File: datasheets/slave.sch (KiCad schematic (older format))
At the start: 22 parts, among them J1 Screw_Terminal_1x02, J2 Screw_Terminal_1x03, Q1 IRFU9024N, Q2 IRFU9024N, Q3 IRFU9024N, U1 PC817, U2 PC817, U3 PC817, U4 nRF24L01, U5 Arduino_Nano

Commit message: Исправление ошибок в схемах
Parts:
- added C1: C, Capacitors_THT:C_Disc_D6.0mm_W2.5mm_P5.00mm, symbol C
- added C2: CP, w_capacitors:CP_5x11mm, symbol CP
- added J3: Screw_Terminal_1x02, w_conn_screw:mors_2p, symbol Screw_Terminal_1x02
- added U6: KA378R33, TO_SOT_Packages_THT:TO-220-4_Vertical, symbol KA378R33
- J1: footprint Connectors_Terminal_Blocks:TerminalBlock_Pheonix_MKDS1.5-2pol -> w_conn_screw:mors_2p
- J2: footprint Connectors_Terminal_Blocks:TerminalBlock_Pheonix_MKDS1.5-3pol -> w_conn_screw:mors_3p
- R1: value R -> 470; footprint Resistors_THT:R_Axial_DIN0207_L6.3mm_D2.5mm_P2.54mm_Vertical -> Resistors_THT:R_Axial_DIN0207_L6.3mm_D2.5mm_P10.16mm_Horizontal
- R2: value R -> 10k
- R3: value R -> 100
- R4, R5: footprint Resistors_THT:R_Axial_DIN0207_L6.3mm_D2.5mm_P2.54mm_Vertical -> Resistors_THT:R_Axial_DIN0207_L6.3mm_D2.5mm_P10.16mm_Horizontal
- U4: footprint (none) -> nRF24x:nRF24L01-NA
- U5: footprint (none) -> arduino:ArduinoNano
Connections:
- net labels added: 3V3, D_VCC
- wire segments 64 -> 77
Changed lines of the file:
@@
 EESchema Schematic File Version 2
+LIBS:slave-rescue
 LIBS:power
 LIBS:device
@@
 Wire Wire Line
 	9400 2850 9500 2850
-NoConn ~ 10250 2450
+NoConn ~ 10250 2850
 Wire Wire Line
 	10150 2250 10150 2450
@@
 F 3 "" H 10050 2650 50  0000 C CNN
 	1    10050 2650
-	1    0    0    -1
+	1    0    0    1
 $EndComp
 Wire Wire Line
@@
 P 8600 2650
 F 0 "R1" V 8680 2650 50  0000 C CNN
-F 1 "R" V 8600 2650 50  0000 C CNN
-F 2 "Resistors_THT:R_Axial_DIN0207_L6.3mm_D2.5mm_P2.54mm_Vertical" V 8530 2650 50  0001 C CNN
+F 1 "470" V 8600 2650 50  0000 C CNN
+F 2 "Resistors_THT:R_Axial_DIN0207_L6.3mm_D2.5mm_P10.16mm_Horizontal" V 8530 2650 50  0001 C CNN
 F 3 "" H 8600 2650 50  0000 C CNN
 	1    8600 2650
@@
 P 9450 2450
 F 0 "R2" V 9530 2450 50  0000 C CNN
-F 1 "R" V 9450 2450 50  0000 C CNN
+F 1 "10k" V 9450 2450 50  0000 C CNN
 F 2 "Resistors_THT:R_Axial_DIN0207_L6.3mm_D2.5mm_P2.54mm_Vertical" V 9380 2450 50  0001 C CNN
 F 3 "" H 9450 2450 50  0000 C CNN
@@
 P 9650 2650
 F 0 "R3" V 9730 2650 50  0000 C CNN
-F 1 "R" V 9650 2650 50  0000 C CNN
+F 1 "100" V 9650 2650 50  0000 C CNN
 F 2 "Resistors_THT:R_Axial_DIN0207_L6.3mm_D2.5mm_P2.54mm_Vertical" V 9580 2650 50  0001 C CNN
 F 3 "" H 9650 2650 50  0000 C CNN
@@
 Wire Wire Line
 	9400 3950 9500 3950
-NoConn ~ 10250 3550
+NoConn ~ 10250 3950
 Wire Wire Line
 	10150 3350 10150 3550
@@
 F 3 "" H 10050 3750 50  0000 C CNN
 	1    10050 3750
-	1    0    0    -1
+	1    0    0    1
 $EndComp
 Wire Wire Line
@@
 F 0 "R4" V 8680 3750 50  0000 C CNN
 F 1 "R" V 8600 3750 50  0000 C CNN
-F 2 "Resistors_THT:R_Axial_DIN0207_L6.3mm_D2.5mm_P2.54mm_Vertical" V 8530 3750 50  0001 C CNN
+F 2 "Resistors_THT:R_Axial_DIN0207_L6.3mm_D2.5mm_P10.16mm_Horizontal" V 8530 3750 50  0001 C CNN
 F 3 "" H 8600 3750 50  0000 C CNN
 	1    8600 3750
@@
 Wire Wire Line
 	9400 5100 9500 5100
-NoConn ~ 10250 4700
+NoConn ~ 10250 5100
 Wire Wire Line
 	10150 4500 10150 4700
@@
 F 3 "" H 10050 4900 50  0000 C CNN
 	1    10050 4900
-	1    0    0    -1
+	1    0    0    1
 $EndComp
 Wire Wire Line
@@
 F 0 "R5" V 8680 4900 50  0000 C CNN
 F 1 "R" V 8600 4900 50  0000 C CNN
-F 2 "Resistors_THT:R_Axial_DIN0207_L6.3mm_D2.5mm_P2.54mm_Vertical" V 8530 4900 50  0001 C CNN
+F 2 "Resistors_THT:R_Axial_DIN0207_L6.3mm_D2.5mm_P10.16mm_Horizontal" V 8530 4900 50  0001 C CNN
 F 3 "" H 8600 4900 50  0000 C CNN
 	1    8600 4900
@@
 P 9200 1300
 F 0 "J1" H 9200 1550 50  0000 C TNN
-F 1 "Screw_Terminal_1x02" V 9050 1300 50  0000 C TNN
-F 2 "Connectors_Terminal_Blocks:TerminalBlock_Pheonix_MKDS1.5-2pol" H 9200 1075 50  0001 C CNN
+F 1 "Screw_Terminal_1x02" V 9050 1300 50  0001 C TNN
+F 2 "w_conn_screw:mors_2p" H 9200 1075 50  0001 C CNN
 F 3 "" H 9175 1300 50  0001 C CNN
 	1    9200 1300
-	-1   0    0    -1
+	-1   0    0    1
 $EndComp
 Wire Wire Line
@@
 P 10300 1400
 F 0 "J2" H 10300 1750 50  0000 C TNN
-F 1 "Screw_Terminal_1x03" V 10150 1400 50  0000 C TNN
-F 2 "Connectors_Terminal_Blocks:TerminalBlock_Pheonix_MKDS1.5-3pol" H 10300 1075 50  0001 C CNN
+F 1 "Screw_Terminal_1x03" V 10150 1400 50  0001 C TNN
+F 2 "w_conn_screw:mors_3p" H 10300 1075 50  0001 C CNN
 F 3 "" H 10275 1500 50  0001 C CNN
 	1    10300 1400
@@
 OUT_1
 Text Label 9800 1200 0    60   ~ 0
-OUT_1
+OUT_3
 Text Label 9800 1400 0    60   ~ 0
 OUT_2
 Text Label 9800 1600 0    60   ~ 0
-OUT_3
+OUT_1
 $Comp
 L Arduino_Nano U5
@@
 F 0 "U5" H 6700 5200 60  0000 C CNN
 F 1 "Arduino_Nano" H 6700 5300 60  0000 C CNN
-F 2 "" H 6700 5200 60  0001 C CNN
+F 2 "arduino:ArduinoNano" H 6700 5200 60  0001 C CNN
 F 3 "" H 6700 5200 60  0001 C CNN
 	1    6700 4400
@@
 	8450 2650 8200 2650
 Text Label 5700 4300 0    60   ~ 0
-IN_1
+IN_3
 Text Label 5700 4400 0    60   ~ 0
 IN_2
 Text Label 5700 4500 0    60   ~ 0
-IN_3
+IN_1
 Text Label 8200 2650 0    60   ~ 0
 IN_1
@@
 Text Label 8200 4900 0    60   ~ 0
 IN_3
-$Comp
-L nRF24L01 U4
-U 1 1 59AE991B
-P 6500 3100
-F 0 "U4" H 6500 3300 60  0000 C CNN
-F 1 "nRF24L01" H 6500 3400 60  0000 C CNN
-F 2 "" H 6500 4050 60  0001 C CNN
-F 3 "" H 6500 4050 60  0001 C CNN
-	1    6500 3100
-	1    0    0    -1
-$EndComp
 Wire Wire Line
 	6000 5100 5700 5100
@@
 NoConn ~ 7400 4000
 NoConn ~ 7400 3900
+$Comp
+L nRF24L01 U4
+U 1 1 59AE849D
+P 6500 3100
+F 0 "U4" H 6500 3450 60  0000 C CNN
+F 1 "nRF24L01" H 6500 3350 60  0000 C CNN
+F 2 "nRF24x:nRF24L01-NA" H 6400 3900 60  0001 C CNN
+F 3 "" H 6400 3900 60  0001 C CNN
+	1    6500 3100
+	1    0    0    -1
+$EndComp
+$Comp
+L Screw_Terminal_1x02 J3
+U 1 1 59AE90CE
+P 8100 1300
+F 0 "J3" H 8100 1550 50  0000 C TNN
+F 1 "Screw_Terminal_1x02" V 7950 1300 50  0001 C TNN
+F 2 "w_conn_screw:mors_2p" H 8100 1075 50  0001 C CNN
+F 3 "" H 8075 1300 50  0001 C CNN
+	1    8100 1300
+	-1   0    0    1
+$EndComp
+Wire Wire Line
+	6000 4000 5700 4000
+Text Label 5700 4000 0    60   ~ 0
+D_GND
+Wire Wire Line
+	7900 1200 7600 1200
+Wire Wire Line
+	7900 1400 7600 1400
+Text Label 7600 1200 0    60   ~ 0
+D_VCC
+Text Label 7600 1400 0    60   ~ 0
+D_GND
+Wire Wire Line
+	7400 3700 7700 3700
+Text Label 7700 3700 2    60   ~ 0
+D_VCC
+Wire Wire Line
+	7000 3000 7300 3000
+Text Label 7300 3000 2    60   ~ 0
+3V3
+$Comp
+L KA378R33 U6
+U 1 1 59AEA7DB
+P 6400 1250
+F 0 "U6" H 6200 1450 50  0000 C CNN
+F 1 "KA378R33" H 6350 1450 50  0000 L CNN
+F 2 "TO_SOT_Packages_THT:TO-220-4_Vertical" H 6400 1350 50  0001 C CIN
+F 3 "" H 6400 1250 50  0001 C CNN
+	1    6400 1250
+	1    0    0    -1
+$EndComp
+Wire Wire Line
+	6000 1200 5700 1200
+Wire Wire Line
+	6800 1200 7100 1200
+Wire Wire Line
+	5700 1350 6000 1350
+Wire Wire Line
+	6400 1550 6400 1850
+Text Label 5700 1200 0    60   ~ 0
+D_VCC
+Text Label 5700 1350 0    60   ~ 0
+D_VCC
+Text Label 7100 1200 2    60   ~ 0
+3V3
+Text Label 6400 1850 1    60   ~ 0
+D_GND
+$Comp
+L CP C2
+U 1 1 59AEA26C
+P 6900 1400
+F 0 "C2" H 6925 1500 50  0000 L CNN
+F 1 "CP" H 6925 1300 50  0000 L CNN
+F 2 "w_capacitors:CP_5x11mm" H 6938 1250 50  0001 C CNN
+F 3 "" H 6900 1400 50  0001 C CNN
+	1    6900 1400
+	1    0    0    -1
+$EndComp
+$Comp
+L C C1
+U 1 1 59AEA4A0
+P 5900 1600
+F 0 "C1" H 5925 1700 50  0000 L CNN
+F 1 "C" H 5925 1500 50  0000 L CNN
+F 2 "Capacitors_THT:C_Disc_D6.0mm_W2.5mm_P5.00mm" H 5938 1450 50  0001 C CNN
+F 3 "" H 5900 1600 50  0001 C CNN
+	1    5900 1600
+	1    0    0    -1
+$EndComp
+Wire Wire Line
+	5900 1450 5900 1350
+Connection ~ 5900 1350
+Wire Wire Line
+	5900 1750 6900 1750
+Connection ~ 6400 1750
+Wire Wire Line
+	6900 1750 6900 1550
+Wire Wire Line
+	6900 1250 6900 1200
+Connection ~ 6900 1200
 $EndSCHEMATC

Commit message: Правка схем
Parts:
- removed U5: Arduino_Nano, arduino:ArduinoNano, symbol Arduino_Nano
- added U5: ArduinoNano, Modules:Arduino_Nano, symbol ArduinoNano
- D1, D2, D3: footprint user_diodes:D_DO-41_SOD81_P12.70mm_Horizontal -> Diodes_THT:D_DO-41_SOD81_P12.70mm_Horizontal
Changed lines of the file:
@@
 EESchema Schematic File Version 2
-LIBS:slave-rescue
 LIBS:power
 LIBS:device
@@
 LIBS:contrib
 LIBS:valves
+LIBS:arduino
+LIBS:nrf
 LIBS:user_transistors
 LIBS:user_diodes
-LIBS:arduino
-LIBS:nrf
 LIBS:slave-cache
-EELAYER 25 0
+EELAYER 26 0
 EELAYER END
 $Descr A4 11693 8268
@@
 Wire Wire Line
 	10150 3250 10150 3300
-Wire Wire Line
-	10150 2850 10150 2950
 $Comp
 L 1N4007 D1
@@
 F 0 "D1" H 10150 3200 50  0000 C CNN
 F 1 "1N4007" H 10150 3000 50  0000 C CNN
-F 2 "user_diodes:D_DO-41_SOD81_P12.70mm_Horizontal" H 10150 3100 50  0001 C CNN
+F 2 "Diodes_THT:D_DO-41_SOD81_P12.70mm_Horizontal" H 10150 3100 50  0001 C CNN
 F 3 "" H 10150 3100 50  0000 C CNN
 	1    10150 3100
@@
 Wire Wire Line
 	10150 4350 10150 4400
-Wire Wire Line
-	10150 3950 10150 4050
 $Comp
 L 1N4007 D2
@@
 F 0 "D2" H 10150 4300 50  0000 C CNN
 F 1 "1N4007" H 10150 4100 50  0000 C CNN
-F 2 "user_diodes:D_DO-41_SOD81_P12.70mm_Horizontal" H 10150 4200 50  0001 C CNN
+F 2 "Diodes_THT:D_DO-41_SOD81_P12.70mm_Horizontal" H 10150 4200 50  0001 C CNN
 F 3 "" H 10150 4200 50  0000 C CNN
 	1    10150 4200
@@
 Wire Wire Line
 	10150 5500 10150 5550
-Wire Wire Line
-	10150 5100 10150 5200
 $Comp
 L 1N4007 D3
@@
 F 0 "D3" H 10150 5450 50  0000 C CNN
 F 1 "1N4007" H 10150 5250 50  0000 C CNN
-F 2 "user_diodes:D_DO-41_SOD81_P12.70mm_Horizontal" H 10150 5350 50  0001 C CNN
+F 2 "Diodes_THT:D_DO-41_SOD81_P12.70mm_Horizontal" H 10150 5350 50  0001 C CNN
 F 3 "" H 10150 5350 50  0000 C CNN
 	1    10150 5350
@@
 Text Label 9800 1600 0    60   ~ 0
 OUT_1
-$Comp
-L Arduino_Nano U5
-U 1 1 59AE7866
-P 6700 4400
-F 0 "U5" H 6700 5200 60  0000 C CNN
-F 1 "Arduino_Nano" H 6700 5300 60  0000 C CNN
-F 2 "arduino:ArduinoNano" H 6700 5200 60  0001 C CNN
-F 3 "" H 6700 5200 60  0001 C CNN
-	1    6700 4400
-	1    0    0    -1
-$EndComp
-Wire Wire Line
-	6000 4300 5700 4300
-Wire Wire Line
-	6000 4400 5700 4400
-Wire Wire Line
-	6000 4500 5700 4500
+Wire Wire Line
+	5700 4300 6200 4300
+Wire Wire Line
+	5700 4400 6200 4400
+Wire Wire Line
+	5700 4500 6200 4500
 Wire Wire Line
 	8450 4900 8200 4900
@@
 IN_3
 Wire Wire Line
-	6000 5100 5700 5100
-Wire Wire Line
-	6000 5000 5700 5000
-Wire Wire Line
-	6000 4900 5700 4900
-Wire Wire Line
-	6000 4800 5700 4800
-Wire Wire Line
-	6000 4100 5700 4100
-Wire Wire Line
-	7400 5100 7700 5100
+	5700 5100 6200 5100
+Wire Wire Line
+	5700 5000 6200 5000
+Wire Wire Line
+	5700 4900 6200 4900
+Wire Wire Line
+	5700 4800 6200 4800
+Wire Wire Line
+	5700 4100 6200 4100
+Wire Wire Line
+	7200 5100 7700 5100
 Wire Wire Line
 	6000 3300 5700 3300
@@
 SCN/D9
 Wire Wire Line
-	7400 3800 7700 3800
+	7200 3800 7700 3800
 Text Label 7700 3800 2    60   ~ 0
 D_GND
@@
 Text Label 5700 3000 0    60   ~ 0
 D_GND
-NoConn ~ 6000 3700
-NoConn ~ 6000 3800
-NoConn ~ 6000 3900
-NoConn ~ 6000 4200
-NoConn ~ 6000 4600
-NoConn ~ 6000 4700
-NoConn ~ 7400 5000
-NoConn ~ 7400 4900
-NoConn ~ 7400 4800
-NoConn ~ 7400 4700
-NoConn ~ 7400 4600
-NoConn ~ 7400 4500
-NoConn ~ 7400 4400
-NoConn ~ 7400 4300
-NoConn ~ 7400 4200
-NoConn ~ 7400 4100
-NoConn ~ 7400 4000
-NoConn ~ 7400 3900
+NoConn ~ 6200 4200
+NoConn ~ 6200 4600
+NoConn ~ 6200 4700
 $Comp
 L nRF24L01 U4
@@
 $EndComp
 Wire Wire Line
-	6000 4000 5700 4000
+	5700 4000 6200 4000
 Text Label 5700 4000 0    60   ~ 0
 D_GND
@@
 D_GND
 Wire Wire Line
-	7400 3700 7700 3700
+	7200 3700 7700 3700
 Text Label 7700 3700 2    60   ~ 0
 D_VCC
@@
 	6900 1250 6900 1200
 Connection ~ 6900 1200
+$Comp
+L ArduinoNano U5
+U 1 1 59BC9DC0
+P 6700 4000
+F 0 "U5" H 6700 4547 60  0000 C CNN
+F 1 "ArduinoNano" H 6700 4441 60  0000 C CNN
+F 2 "Modules:Arduino_Nano" H 6650 4550 60  0001 C CNN
+F 3 "" H 6650 4550 60  0001 C CNN
+	1    6700 4000
+	1    0    0    -1
+$EndComp
+NoConn ~ 6200 3700
+NoConn ~ 6200 3800
+NoConn ~ 6200 3900
+NoConn ~ 7200 5000
+NoConn ~ 7200 4900
+NoConn ~ 7200 4800
+NoConn ~ 7200 4700
+NoConn ~ 7200 4600
+NoConn ~ 7200 4500
+NoConn ~ 7200 4400
+NoConn ~ 7200 4300
+NoConn ~ 7200 4200
+NoConn ~ 7200 4100
+NoConn ~ 7200 4000
+NoConn ~ 7200 3900
+Wire Wire Line
+	10150 5100 10150 5200
+Wire Wire Line
+	10150 3950 10150 4050
+Wire Wire Line
+	10150 2850 10150 2950
 $EndSCHEMATC

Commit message: Добавление библиотек компонентов для KiCad.
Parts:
- J1, J3: symbol Screw_Terminal_1x02 -> Screw_Terminal_01x02
- J2: symbol Screw_Terminal_1x03 -> Screw_Terminal_01x03
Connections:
- wire segments 77 -> 78
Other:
- moved on the sheet: C2
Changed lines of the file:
@@
 LIBS:arduino
 LIBS:nrf
+LIBS:user_diodes
 LIBS:user_transistors
-LIBS:user_diodes
 LIBS:slave-cache
-EELAYER 26 0
+EELAYER 25 0
 EELAYER END
 $Descr A4 11693 8268
@@
 P_VCC
 $Comp
-L Screw_Terminal_1x02 J1
+L Screw_Terminal_01x02 J1
 U 1 1 59ADE9CB
 P 9200 1300
@@
 F 3 "" H 9175 1300 50  0001 C CNN
 	1    9200 1300
-	-1   0    0    1
+	1    0    0    1
 $EndComp
 Wire Wire Line
 	9000 1200 8700 1200
 Wire Wire Line
-	9000 1400 8700 1400
+	9000 1300 8700 1300
 Text Label 8700 1200 0    60   ~ 0
 P_VCC
-Text Label 8700 1400 0    60   ~ 0
-P_GND
-$Comp
-L Screw_Terminal_1x03 J2
-U 1 1 59AE55A4
-P 10300 1400
-F 0 "J2" H 10300 1750 50  0000 C TNN
-F 1 "Screw_Terminal_1x03" V 10150 1400 50  0001 C TNN
-F 2 "w_conn_screw:mors_3p" H 10300 1075 50  0001 C CNN
-F 3 "" H 10275 1500 50  0001 C CNN
-	1    10300 1400
-	-1   0    0    1
-$EndComp
-Wire Wire Line
-	10100 1200 9700 1200
-Wire Wire Line
-	10100 1400 9700 1400
-Wire Wire Line
-	10100 1600 9700 1600
+Text Label 8700 1300 0    60   ~ 0
+P_GND
+Wire Wire Line
+	10050 1200 9650 1200
+Wire Wire Line
+	10050 1300 9650 1300
+Wire Wire Line
+	10050 1400 9650 1400
 Wire Wire Line
 	10150 2900 10550 2900
@@
 Text Label 10250 2900 0    60   ~ 0
 OUT_1
-Text Label 9800 1200 0    60   ~ 0
+Text Label 9750 1200 0    60   ~ 0
 OUT_3
-Text Label 9800 1400 0    60   ~ 0
+Text Label 9750 1300 0    60   ~ 0
 OUT_2
-Text Label 9800 1600 0    60   ~ 0
+Text Label 9750 1400 0    60   ~ 0
 OUT_1
 Wire Wire Line
@@
 $EndComp
 $Comp
-L Screw_Terminal_1x02 J3
+L Screw_Terminal_01x02 J3
 U 1 1 59AE90CE
 P 8100 1300
@@
 F 3 "" H 8075 1300 50  0001 C CNN
 	1    8100 1300
-	-1   0    0    1
+	1    0    0    1
 $EndComp
 Wire Wire Line
@@
 	7900 1200 7600 1200
 Wire Wire Line
-	7900 1400 7600 1400
+	7900 1300 7600 1300
 Text Label 7600 1200 0    60   ~ 0
 D_VCC
-Text Label 7600 1400 0    60   ~ 0
+Text Label 7600 1300 0    60   ~ 0
 D_GND
 Wire Wire Line
@@
 $EndComp
 Wire Wire Line
-	6000 1200 5700 1200
-Wire Wire Line
-	6800 1200 7100 1200
-Wire Wire Line
-	5700 1350 6000 1350
+	5700 1150 6100 1150
+Wire Wire Line
+	6700 1150 7100 1150
+Wire Wire Line
+	5700 1300 6100 1300
 Wire Wire Line
 	6400 1550 6400 1850
-Text Label 5700 1200 0    60   ~ 0
+Text Label 5700 1150 0    60   ~ 0
 D_VCC
-Text Label 5700 1350 0    60   ~ 0
+Text Label 5700 1300 0    60   ~ 0
 D_VCC
-Text Label 7100 1200 2    60   ~ 0
+Text Label 7100 1150 2    60   ~ 0
 3V3
 Text Label 6400 1850 1    60   ~ 0
@@
 L CP C2
 U 1 1 59AEA26C
-P 6900 1400
-F 0 "C2" H 6925 1500 50  0000 L CNN
-F 1 "CP" H 6925 1300 50  0000 L CNN
-F 2 "w_capacitors:CP_5x11mm" H 6938 1250 50  0001 C CNN
-F 3 "" H 6900 1400 50  0001 C CNN
-	1    6900 1400
+P 6900 1350
+F 0 "C2" H 6925 1450 50  0000 L CNN
+F 1 "CP" H 6925 1250 50  0000 L CNN
+F 2 "w_capacitors:CP_5x11mm" H 6938 1200 50  0001 C CNN
+F 3 "" H 6900 1350 50  0001 C CNN
+	1    6900 1350
 	1    0    0    -1
 $EndComp
@@
 $EndComp
 Wire Wire Line
-	5900 1450 5900 1350
-Connection ~ 5900 1350
+	5900 1300 5900 1450
+Connection ~ 5900 1300
 Wire Wire Line
 	5900 1750 6900 1750
 Connection ~ 6400 1750
 Wire Wire Line
-	6900 1750 6900 1550
-Wire Wire Line
-	6900 1250 6900 1200
-Connection ~ 6900 1200
+	6900 1750 6900 1500
+Wire Wire Line
+	6900 1200 6900 1150
+Connection ~ 6900 1150
 $Comp
 L ArduinoNano U5
@@
 Wire Wire Line
 	10150 2850 10150 2950
+Wire Wire Line
+	6100 1300 6100 1250
+$Comp
+L Screw_Terminal_01x03 J2
+U 1 1 59AE55A4
+P 10250 1300
+F 0 "J2" H 10250 1650 50  0000 C TNN
+F 1 "Screw_Terminal_1x03" V 10100 1300 50  0001 C TNN
+F 2 "w_conn_screw:mors_3p" H 10250 975 50  0001 C CNN
+F 3 "" H 10225 1400 50  0001 C CNN
+	1    10250 1300
+	1    0    0    1
+$EndComp
 $EndSCHEMATC

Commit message: Добавил 3D модели
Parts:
- U5: footprint Modules:Arduino_Nano -> arduino:ArduinoNano
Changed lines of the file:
@@
 F 0 "U5" H 6700 4547 60  0000 C CNN
 F 1 "ArduinoNano" H 6700 4441 60  0000 C CNN
-F 2 "Modules:Arduino_Nano" H 6650 4550 60  0001 C CNN
+F 2 "arduino:ArduinoNano" H 6650 4550 60  0001 C CNN
 F 3 "" H 6650 4550 60  0001 C CNN
 	1    6700 4000

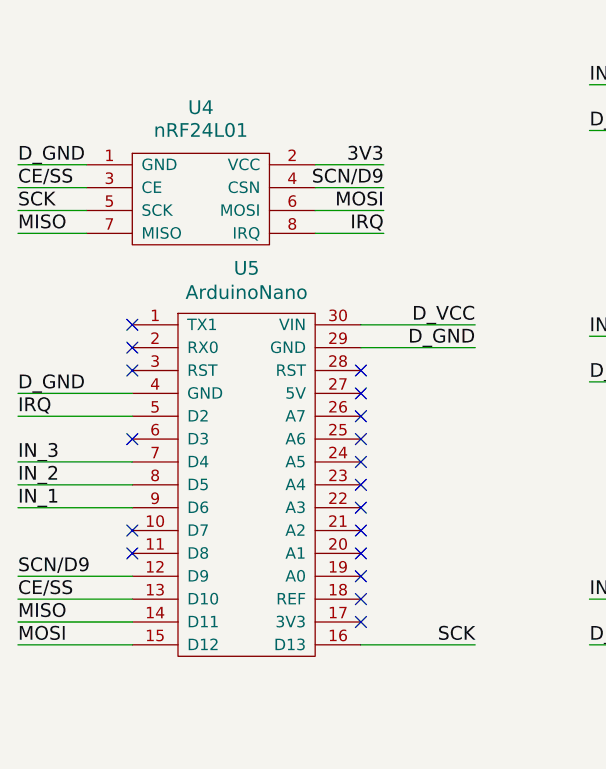
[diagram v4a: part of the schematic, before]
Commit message: Исправление ошибок. Неправильные MOSI и MISO
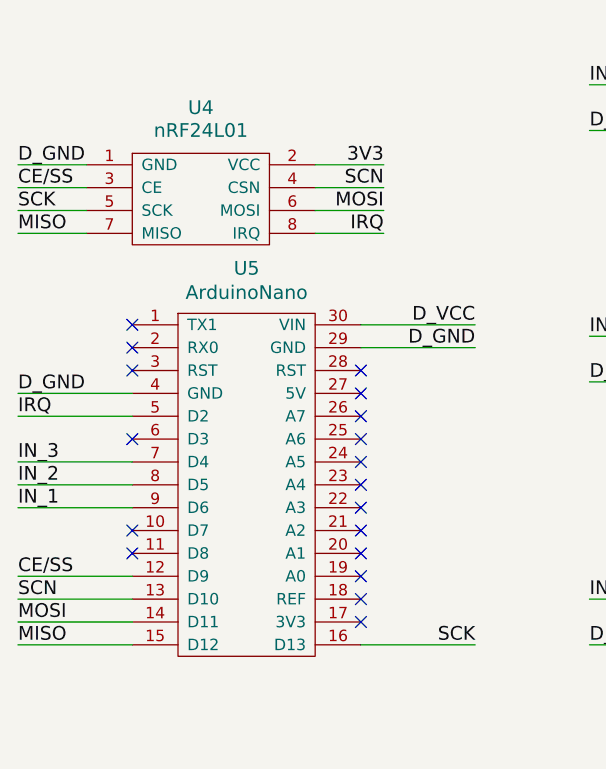
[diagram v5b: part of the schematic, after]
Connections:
- net labels added: SCN
- net labels removed: SCN/D9
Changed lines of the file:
@@
 	7000 3100 7300 3100
 Text Label 5700 5000 0    60   ~ 0
-MISO
-Text Label 5700 5100 0    60   ~ 0
 MOSI
 Text Label 7700 5100 2    60   ~ 0
@@
 MOSI
 Text Label 5700 4900 0    60   ~ 0
-CE/SS
+SCN
 Wire Wire Line
 	6000 3100 5700 3100
@@
 CE/SS
 Text Label 7300 3100 2    60   ~ 0
-SCN/D9
+SCN
 Text Label 5700 4800 0    60   ~ 0
-SCN/D9
+CE/SS
 Wire Wire Line
 	7200 3800 7700 3800
@@
 	1    0    0    1
 $EndComp
+Text Label 5700 5100 0    60   ~ 0
+MISO
 $EndSCHEMATC

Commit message: Правка схем. Наведение красивости.
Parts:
- C1: value C -> 100nF
- C2: value CP -> 10uF
- R4, R5: value R -> 470
- R6, R7: value R -> 10k
- R8, R9: value R -> 100
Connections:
- wire segments 78 -> 91
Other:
- moved on the sheet: C1, C2, D1, D2, D3, J1, J2, J3, Q1, Q2, Q3, R1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
